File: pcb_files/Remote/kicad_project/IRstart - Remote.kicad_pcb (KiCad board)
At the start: 2 copper layers, 40 x 59.4 mm, 53 parts, among them SW1 SW_DIP_x02, SW2 SW_DIP_x02, SW3 SW_DPDT_x2

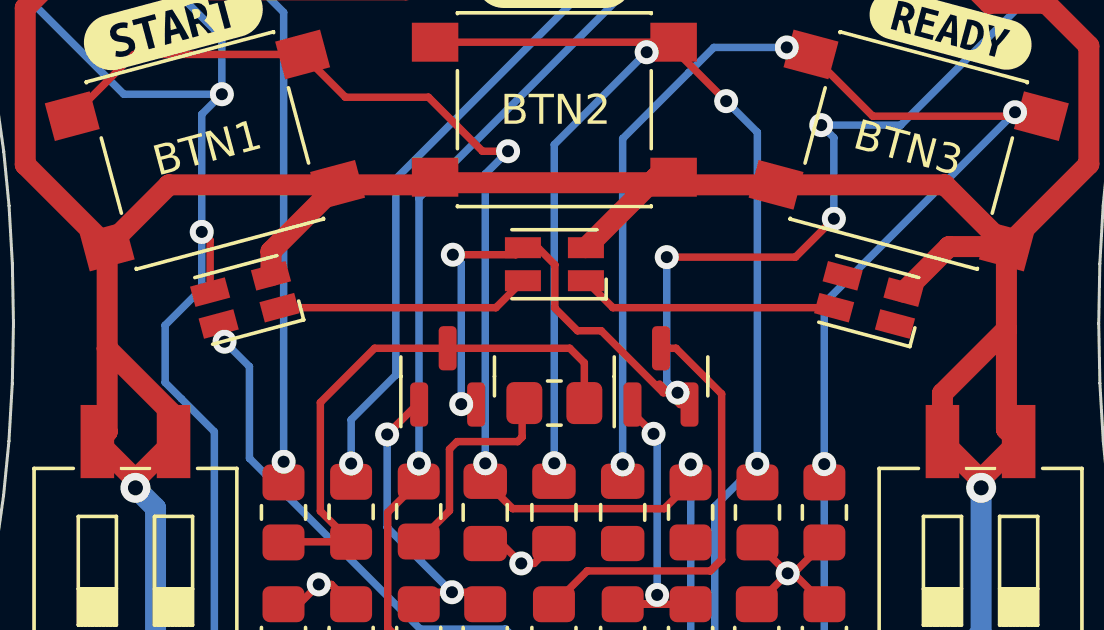
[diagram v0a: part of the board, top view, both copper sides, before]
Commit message: Corrige leds RGB con huella incorrecta
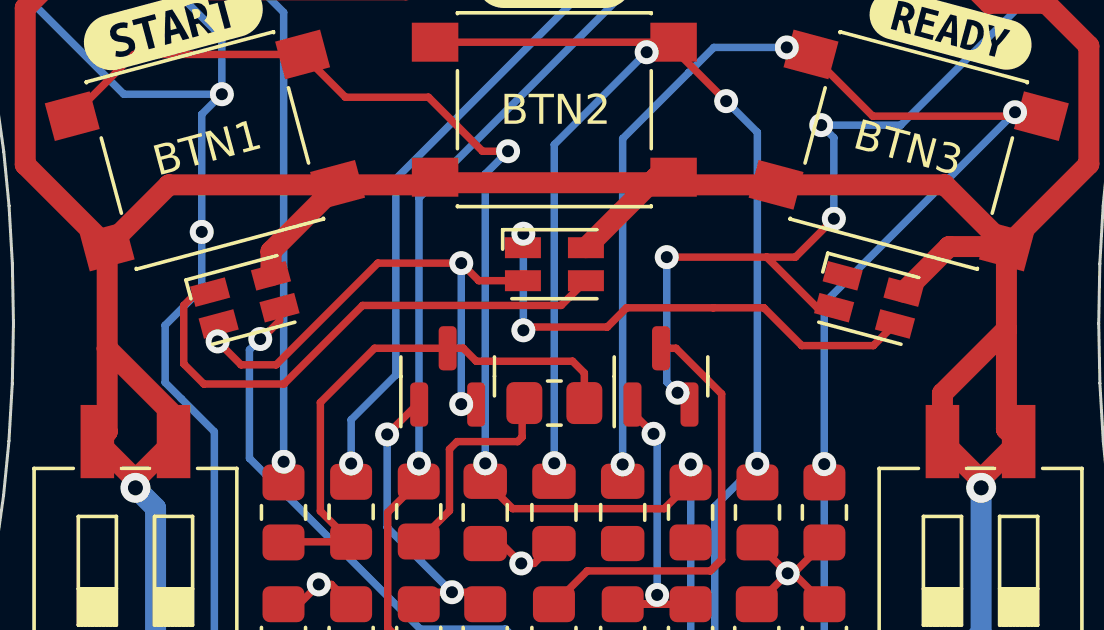
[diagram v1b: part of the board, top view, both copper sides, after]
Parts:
- turned NEO1 to 15 degrees
- turned NEO2 to 0 degrees
- turned NEO3 to -15 degrees
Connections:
- NEO1 pad 2: +3.3V -> GND
- NEO1 pad 3: GND -> /RGBs
- NEO1 pad 4: /RGBs -> +3.3V
- NEO2 pad 2: +3.3V -> GND
- NEO2 pad 3: GND -> Net-(NEO1-DOUT)
- NEO2 pad 4: Net-(NEO1-DOUT) -> +3.3V
- NEO3 pad 2: +3.3V -> GND
- NEO3 pad 3: GND -> Net-(NEO2-DOUT)
- NEO3 pad 4: Net-(NEO2-DOUT) -> +3.3V
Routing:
- net Net-(NEO1-DOUT): track 8.49 -> 18.1 mm
- net Net-(NEO2-DOUT): track 8.65 -> 17.2 mm, vias 0 -> 2
- net GND: track 181.3 -> 182.8 mm, vias 24 -> 25
- net /RGBs: track 43.6 -> 44.2 mm

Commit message: Crea la Rev.2 del mando añadiendo boton de modo y lectura de bateria
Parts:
- removed kibuzzard-6637BADB: G***, kibuzzard-6637BADB
- removed kibuzzard-6637BD08: G***, kibuzzard-6637BD08
- added BTN4: ~, Button_Switch_SMD:SW_SPST_B3U-1000P, F.Cu at (153.5, 94.5)
- added R20: 10k, Resistor_SMD:R_0805_2012Metric_Pad1.20x1.40mm_HandSolder, F.Cu at (141.3, 110.8)
- added kibuzzard-673F80D1: G***, kibuzzard-673F80D1, F.Cu at (153.5, 92.2)
- added kibuzzard-673F8949: G***, kibuzzard-673F8949, F.Cu at (166.6, 82.0)
- added kibuzzard-673F8963: G***, kibuzzard-673F8963, F.Cu at (140.7, 82.0)
- R1, R2, R3: value 150 -> 10
- R12: value 47K -> 100K
- R19: value 0 -> 27k
- moved R19 23.4 mm to (141.3, 114.5), turned to -90 degrees
- moved R4 14.4 mm to (140.3, 125.7)
- moved R5 9.87 mm to (142.3, 125.7), turned to 90 degrees
- moved LDO1 1.47 mm to (141.3, 121.0)
- moved MOSFET2 1.36 mm to (158.4, 94.1)
- moved MOSFET1 1.36 mm to (148.7, 94.1)
- moved D2 0.35 mm to (136.0, 122.9)
- moved D1 0.35 mm to (136.0, 120.7)
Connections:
- ESP1 pad 14: /SWITCH3 -> /ANALOG_BATT
- ESP1 pad 2: unconnected-(ESP1-6-Pad2) -> /BTN_MODO
- ESP1 pad 5: unconnected-(ESP1-9-Pad5) -> /SWITCH3
- R19 pad 1: Net-(R19-Pad1) -> /ANALOG_BATT
- R19 pad 2: Net-(MOSFET1-D) -> /BATT
- R3 pad 2: Net-(R19-Pad1) -> Net-(MOSFET1-D)
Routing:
- net /BTN_MODO: track 0.00 -> 33.4 mm, vias 0 -> 2
- net +5V: track 68.4 -> 45.8 mm, vias 7 -> 3
- net Net-(D1-A): track 27.4 -> 11.9 mm
- net /ANALOG_BATT: track 0.00 -> 11.7 mm
- net +3.3V: track 202.3 -> 190.8 mm, vias 6 -> 7
- net Net-(D2-A): track 20.8 -> 9.50 mm, vias 2 -> 0
- net Net-(R19-Pad1): track 7.26 -> 0.00 mm
- net /BATT: track 63.3 -> 68.5 mm, vias 2 -> 3
- net Net-(MOSFET1-D): track 18.2 -> 13.9 mm, vias 0 -> 2
- net GND: track 182.8 -> 187.0 mm, vias 25 -> 30
- net /SWITCH3: track 26.0 -> 30.1 mm, vias 0 -> 2
- net Net-(LDO1-CE): track 16.5 -> 19.6 mm
- net Net-(NEO2-DOUT): track 17.2 -> 19.5 mm
- net /START_BTN: track 49.6 -> 51.3 mm
- net Net-(MOSFET2-D): track 14.4 -> 13.4 mm
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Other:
- board text added: "Rev.2"
